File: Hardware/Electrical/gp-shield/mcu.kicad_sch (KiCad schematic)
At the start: 36 parts

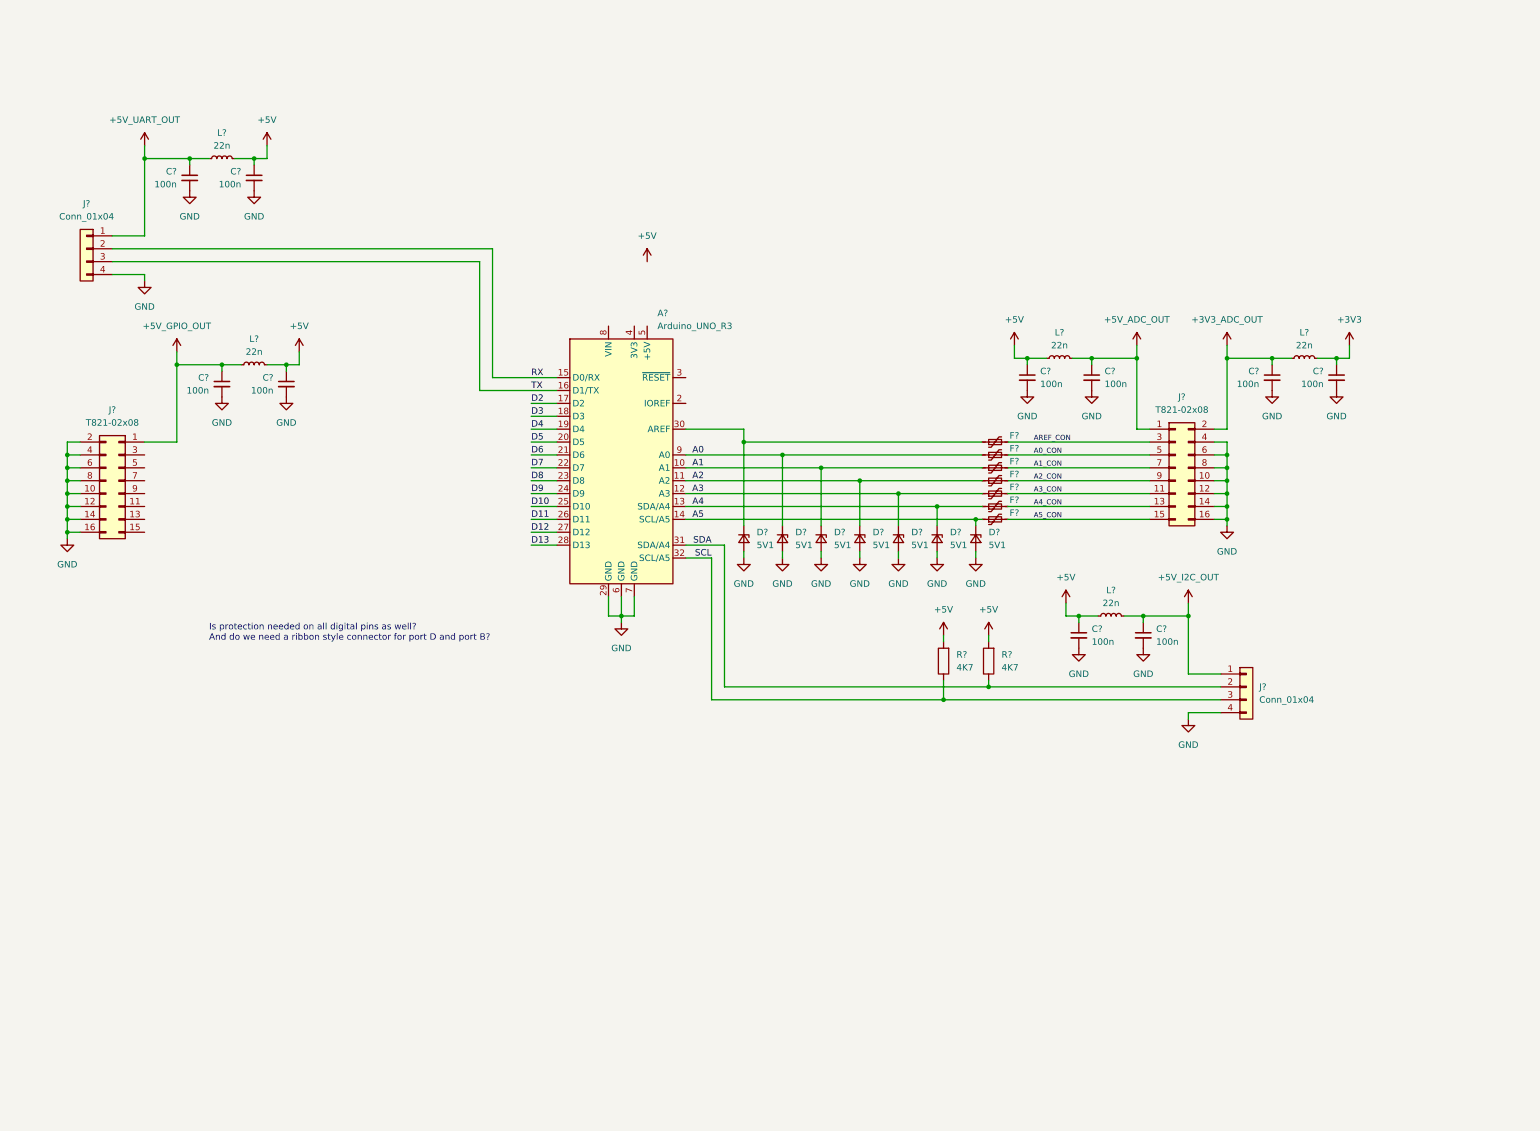
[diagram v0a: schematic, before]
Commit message: Added PWM connectors, subnet labels, arduino power supply protection
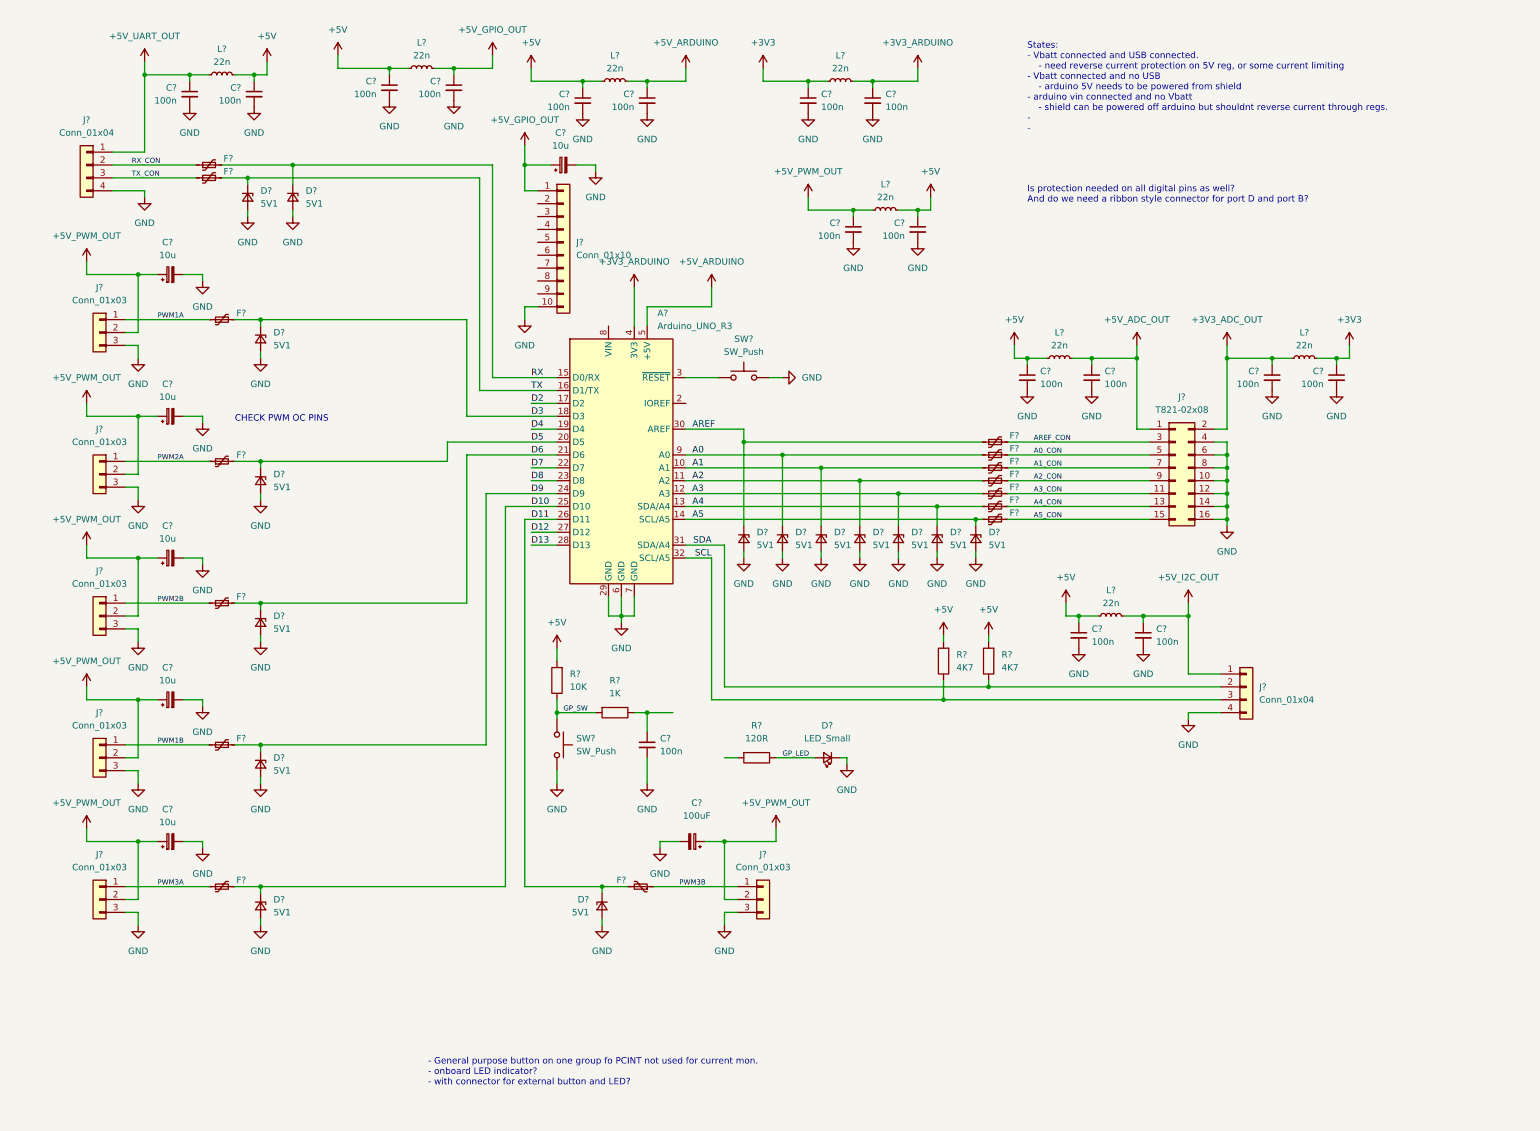
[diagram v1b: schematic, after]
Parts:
- removed C? (x2): 100n, symbol Device:C_Small
- removed J?: T821-02x08, symbol Connector_Generic:Conn_02x08_Odd_Even
- removed L?: 22n, symbol Device:L_Small
- added C? (x9): 100n, symbol Device:C_Small
- added C? (x6): 10u, symbol Device:C_Polarized_Small
- added C?: 100uF, symbol Device:C_Polarized_Small
- added D? (x8): 5V1, symbol Device:D_Zener_Small
- added D?: LED_Small, symbol Device:LED_Small
- added F? (x8): Polyfuse_Small, symbol Device:Polyfuse_Small
- added J? (x6): Conn_01x03, symbol Connector_Generic:Conn_01x03
- added J?: Conn_01x10, symbol Connector_Generic:Conn_01x10
- added L? (x4): 22n, symbol Device:L_Small
- added R?: 1K, symbol Device:R
- added R?: 10K, symbol Device:R
- added R?: 120R, symbol Device:R
- added SW? (x2): SW_Push, symbol Switch:SW_Push
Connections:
- net +3V3: now also C?.1, L?.1
- net +5V: now also C?.1, C?.1, C?.1, L?.1, L?.2, L?.2, R?.2
- net +5V_ADC_OUT: now also C?.1, C?.1, J?.1 (Pin_1), L?.1
- net D10: now also D?.1 (K), F?.2
- net D11: now also D?.1 (K), F?.2
- net D3: now also D?.1 (K), F?.2
- net D5: now also D?.1 (K), F?.2
- net D6: now also D?.1 (K), F?.2
- net D9: now also D?.1 (K), F?.2
- net GND: now also C?.2, C?.2, C?.2, C?.2, C?.2, C?.2, C?.2, C?.2, C?.2, C?.2, C?.2, C?.2, C?.2, C?.2, C?.2, C?.2, D?.1 (K), D?.2 (A), D?.2 (A), D?.2 (A), D?.2 (A), D?.2 (A), D?.2 (A), D?.2 (A), D?.2 (A), J?.10 (Pin_10), J?.3 (Pin_3), J?.3 (Pin_3), J?.3 (Pin_3), J?.3 (Pin_3), J?.3 (Pin_3), J?.3 (Pin_3), SW?.2, SW?.2
- net RX: now also D?.1 (K), F?.2; no longer J?.2 (Pin_2)
- net TX: now also D?.1 (K), F?.2; no longer J?.3 (Pin_3)
- net AREF: now reaches A?.30 (AREF), D?.1 (K), F?.1
- net at A?.3 (~{RESET}): now also SW?.1
- net +3V3_ARDUINO: now reaches A?.4 (3V3)
- net +3V3_ARDUINO: now also C?.1, L?.2
- net +5V_ARDUINO: now reaches A?.5 (+5V)
- net +5V_ARDUINO: now also C?.1, L?.1
- new net: C?.1, R?.1
- new net +5V_PWM_OUT: C?.1, C?.1, C?.1, C?.1, C?.1, C?.1, C?.1, J?.2 (Pin_2), J?.2 (Pin_2), J?.2 (Pin_2), J?.2 (Pin_2), J?.2 (Pin_2), J?.2 (Pin_2), L?.2
- new net GP_LED: D?.2 (A), R?.1
- new net GP_SW: R?.1, R?.2, SW?.1
- new net PWM1A: F?.1, J?.1 (Pin_1)
- new net PWM1B: F?.1, J?.1 (Pin_1)
- new net PWM2A: F?.1, J?.1 (Pin_1)
- new net PWM2B: F?.1, J?.1 (Pin_1)
- new net PWM3A: F?.1, J?.1 (Pin_1)
- new net PWM3B: F?.1, J?.1 (Pin_1)
- new net RX_CON: F?.1, J?.2 (Pin_2)
- new net TX_CON: F?.1, J?.3 (Pin_3)
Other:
- note added: "- General purpose button on one group fo PCINT not used for current mon. - onboard LED indicator? - with connector for external button and LED?"
- note added: "CHECK PWM OC PINS"
- note added: "States: - Vbatt connected and USB connected. - need reverse current protection on 5V reg, or some current limiting - Vbatt connected and no USB - arduino 5V needs to be powered from shield - arduino vin connected and no Vbatt - shield can be powered off arduino but shouldnt reverse current through regs. - -"
- moved on the sheet: C?, J?, L?

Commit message: Major revisions to PCB layout
- near final layout
- prototype version of silkscreen
- removed 3.3V reg
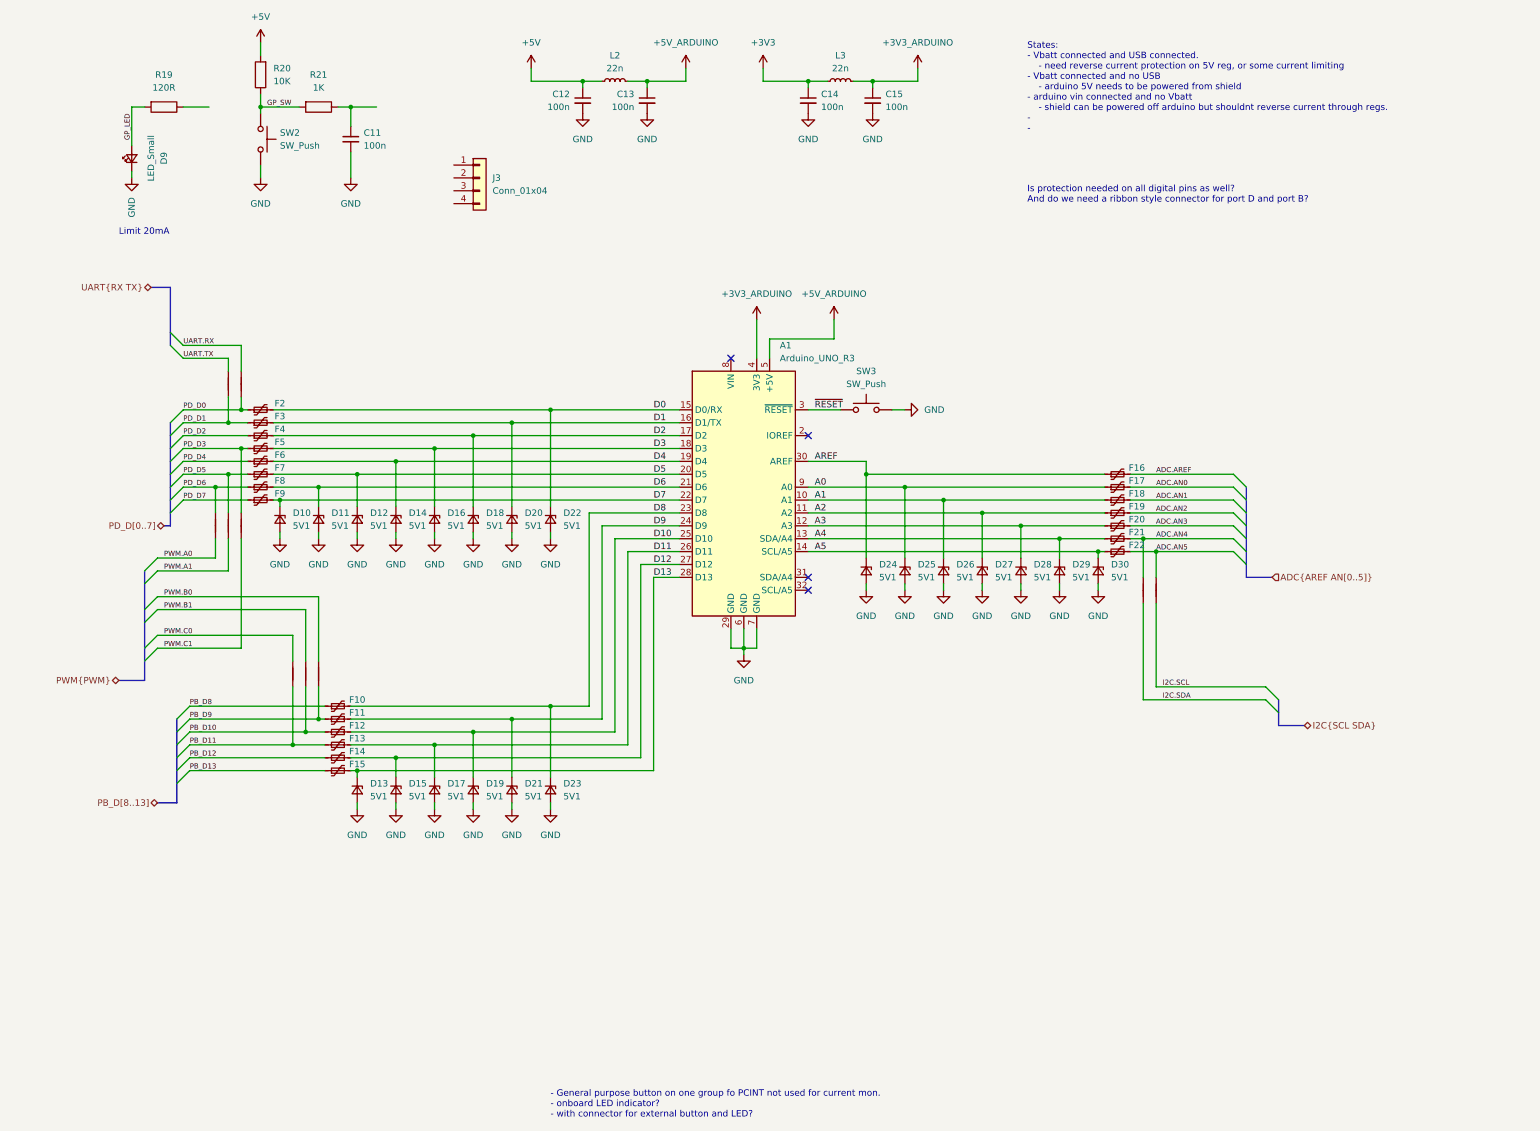
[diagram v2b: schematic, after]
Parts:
- removed C? (x12): 100n, symbol Device:C_Small
- removed C? (x6): 10u, symbol Device:C_Polarized_Small
- removed C?: 100uF, symbol Device:C_Polarized_Small
- removed D? (x8): 5V1, symbol Device:D_Zener_Small
- removed F? (x8): Polyfuse_Small, symbol Device:Polyfuse_Small
- removed J? (x6): Conn_01x03, symbol Connector_Generic:Conn_01x03
- removed J? (x2): Conn_01x04, symbol Connector_Generic:Conn_01x04
- removed J?: Conn_01x10, symbol Connector_Generic:Conn_01x10
- removed J?: T821-02x08, symbol Connector_Generic:Conn_02x08_Odd_Even
- removed L? (x6): 22n, symbol Device:L_Small
- removed R? (x2): 4K7, symbol Device:R
- added D10, D11, D12, D13, D14, D15, D16, D17, D18, D19, D20, D21, D22, D23: 5V1, Diode_SMD:D_0805_2012Metric_Pad1.15x1.40mm_HandSolder, symbol Device:D_Zener_Small
- added F10, F11, F12, F13, F14, F15, F2, F3, F4, F5, F6, F7, F8, F9: Polyfuse_Small, Fuse:Fuse_0603_1608Metric_Pad1.05x0.95mm_HandSolder, symbol Device:Polyfuse_Small
- added J3: Conn_01x04, Connector_Molex:Molex_KK-254_AE-6410-04A_1x04_P2.54mm_Vertical, symbol Connector_Generic:Conn_01x04
- added NT1, NT10, NT2, NT3, NT4, NT5, NT6, NT7, NT8, NT9: NetTie_2, NetTie:NetTie-2_THT_Pad0.3mm, symbol Device:NetTie_2
- C11, C12, C13, C14, C15: renamed from C?; footprint (none) -> Capacitor_SMD:C_0805_2012Metric_Pad1.18x1.45mm_HandSolder
- D24, D25, D26, D27, D28, D29, D30: renamed from D?; footprint (none) -> Diode_SMD:D_0805_2012Metric_Pad1.15x1.40mm_HandSolder
- D9: renamed from D?; footprint (none) -> LED_SMD:LED_0805_2012Metric_Pad1.15x1.40mm_HandSolder
- F16, F17, F18, F19, F20, F21, F22: renamed from F?; footprint (none) -> Fuse:Fuse_0603_1608Metric_Pad1.05x0.95mm_HandSolder; Digikey Part No (none) -> PRG18BB221MB1RB
- L2, L3: renamed from L?; footprint (none) -> Inductor_SMD:L_0805_2012Metric_Pad1.15x1.40mm_HandSolder
- R19, R20, R21: renamed from R?; footprint (none) -> Resistor_SMD:R_0805_2012Metric_Pad1.20x1.40mm_HandSolder
- SW2, SW3: renamed from SW?; footprint (none) -> Button_Switch_THT:SW_TH_Tactile_Omron_B3F-10xx
- gave numbers to parts that had none: 1
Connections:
- net D10: now also D19.1 (K), F12.2
- net D11: now also D17.1 (K), F13.2
- net D12: now also D15.1 (K), F14.2
- net D13: now also D13.1 (K), F15.2
- net D2: now also D18.1 (K), F4.2
- net D3: now also D16.1 (K), F5.2
- net D4: now also D14.1 (K), F6.2
- net D5: now also D12.1 (K), F7.2
- net D6: now also D11.1 (K), F8.2
- net D7: now also D10.1 (K), F9.2
- net D8: now also D23.1 (K), F10.2
- net D9: now also D21.1 (K), F11.2
- net GND: now also D10.2 (A), D11.2 (A), D12.2 (A), D13.2 (A), D14.2 (A), D15.2 (A), D16.2 (A), D17.2 (A), D18.2 (A), D19.2 (A), D20.2 (A), D21.2 (A), D22.2 (A), D23.2 (A)
- net GP_LED: now also R19.2; no longer R19.1
- net ~{RESET}: now reaches A1.3 (~{RESET}), SW3.1
- net A0_CON renamed ADC.AN0
- net A1_CON renamed ADC.AN1
- net A2_CON renamed ADC.AN2
- net A3_CON renamed ADC.AN3
- net A4_CON renamed ADC.AN4
- net ADC.AN4: now also NT9.2
- net A5_CON renamed ADC.AN5
- net ADC.AN5: now also NT10.2
- net AREF_CON renamed ADC.AREF
- net RX renamed D0
- net D0: now also D22.1 (K), F2.2
- net SCL: no longer names the net of A1.32 (SCL/A5)
- net SDA: no longer names the net of A1.31 (SDA/A4)
- net TX renamed D1
- net D1: now also D20.1 (K), F3.2
- new net I2C.SCL: NT10.1
- new net I2C.SDA: NT9.1
- new net PB_D10: F12.1, NT7.1
- new net PB_D11: F13.1, NT6.1
- new net PB_D12: F14.1
- new net PB_D13: F15.1
- new net PB_D8: F10.1
- new net PB_D9: F11.1, NT8.1
- new net PD_D0: F2.1, NT4.1
- new net PD_D1: F3.1, NT2.1
- new net PD_D2: F4.1
- new net PD_D3: F5.1, NT5.2
- new net PD_D4: F6.1
- new net PD_D5: F7.1, NT3.2
- new net PD_D6: F8.1, NT1.2
- new net PD_D7: F9.1
- new net PWM.A0: NT1.1
- new net PWM.A1: NT3.1
- new net PWM.B0: NT8.2
- new net PWM.B1: NT7.2
- new net PWM.C0: NT6.2
- new net PWM.C1: NT5.1
- new net UART.RX: NT4.2
- new net UART.TX: NT2.2
- no-connect marks 0 -> 4
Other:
- note added: "Limit 20mA"
- note removed: "CHECK PWM OC PINS"
- moved on the sheet: A1, C11, D24, D25, D26, D27, D28, D29, D30, D9, F16, F17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
